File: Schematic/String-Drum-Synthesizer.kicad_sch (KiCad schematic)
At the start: 47 parts, among them J1 USB_A, J2 USB_A, J3 HDMI_A_1.4, U1 LM1117MP-3.3, U2 SII1136CTU, U4 LM3900DR, U5 LM1117MP-3.3, U6 STM32F722RCTx

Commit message: Schematic Done!!
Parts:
- removed C10: 4.7uF, symbol Device:C_Polarized
- added R18, R20, R22: 4k7, symbol Device:R
- added R19, R21, R23: 10k, symbol Device:R
- added R24, R25, R26: 1M, symbol Device:R
- added U3: 74LS257, symbol 74xx:74LS257
- renumbered AudioJack to AudioJack1, J1 to KeyboardUSBPort, J2 to ProgrammingUSBPort
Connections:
- net +5V: now also U3.16 (VCC), U3.2 (I0a); no longer J3.18 (+5V)
- net GND: now also R19.1, R21.1, R23.1, R24.1, R25.1, R26.1, U3.10 (I1d), U3.11 (I0d), U3.13 (I1c), U3.14 (I0c), U3.3 (I1a), U3.5 (I0b), U3.6 (I1b), U3.8 (GND)
- net PB10: now also U6.28 (PB10)
- net PB11: now also U6.29 (PB11)
- net PB2: now also U6.27 (PB2)
- net PB3: now also U6.55 (PB3)
- net PB4: now also U6.56 (PB4)
- net PB5: now also U6.57 (PB5)
- net PB6: now also U6.58 (PB6)
- net PB7: now also U6.59 (PB7)
- net PB8: now also U6.61 (PB8)
- net PB9: now also U6.62 (PB9)
- net PC0: now also U6.8 (PC0)
- net PC1: now also U6.9 (PC1)
- net PC13: now also U6.2 (PC13)
- net PC2: now also U6.10 (PC2)
- net USB_OTG_FS_DM: now also R10.2, R8.1; no longer KeyboardUSBPort.2 (D-)
- net USB_OTG_FS_DP: now also R22.1, R23.2; no longer KeyboardUSBPort.3 (D+)
- net USB_OTG_HS_DM: now also R20.1, R21.2; no longer ProgrammingUSBPort.2 (D-)
- net USB_OTG_HS_DP: now also R18.1, R19.2; no longer ProgrammingUSBPort.3 (D+)
- net HDMI_PWR: now reaches U6.50 (PA15)
- net HDMI_PWR: now also J3.18 (+5V), U3.4 (Za)
- net at R8.2: now also KeyboardUSBPort.2 (D-); no longer ProgrammingUSBPort.1 (VBUS)
- net USB_OTG_FS_VBUS: no longer names the net of U6.42 (PA9)
- removed net USB_OTG_HS_VBUS: R10.2, R8.1, U6.34 (PB13)
- new net: KeyboardUSBPort.3 (D+), R22.2
- new net: ProgrammingUSBPort.3 (D+), R18.2
- new net: R26.2, U3.9 (Zd)
- new net: ProgrammingUSBPort.2 (D-), R20.2
- new net: R25.2, U3.12 (Zc)
- new net: R24.2, U3.7 (Zb)
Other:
- moved on the sheet: ProgrammingUSBPort

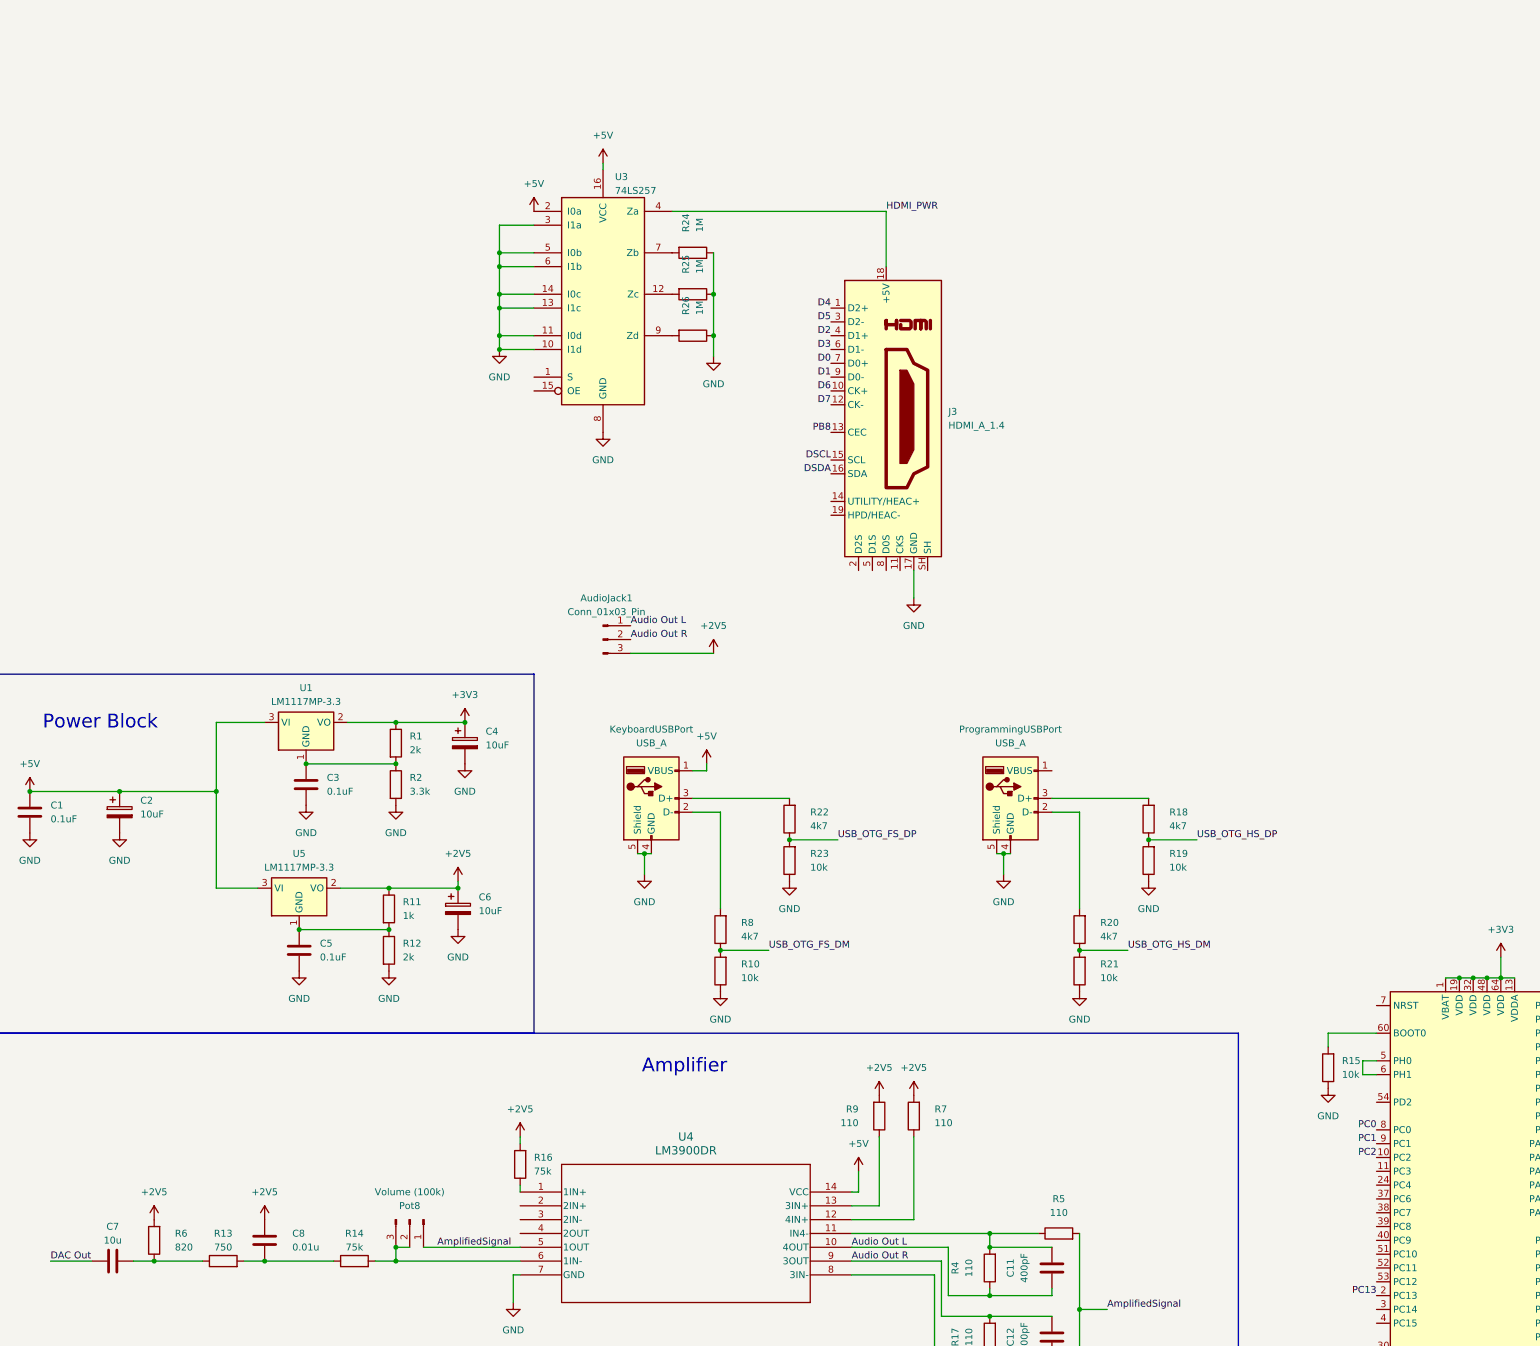
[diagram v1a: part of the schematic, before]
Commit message: Needs R and C Footprints
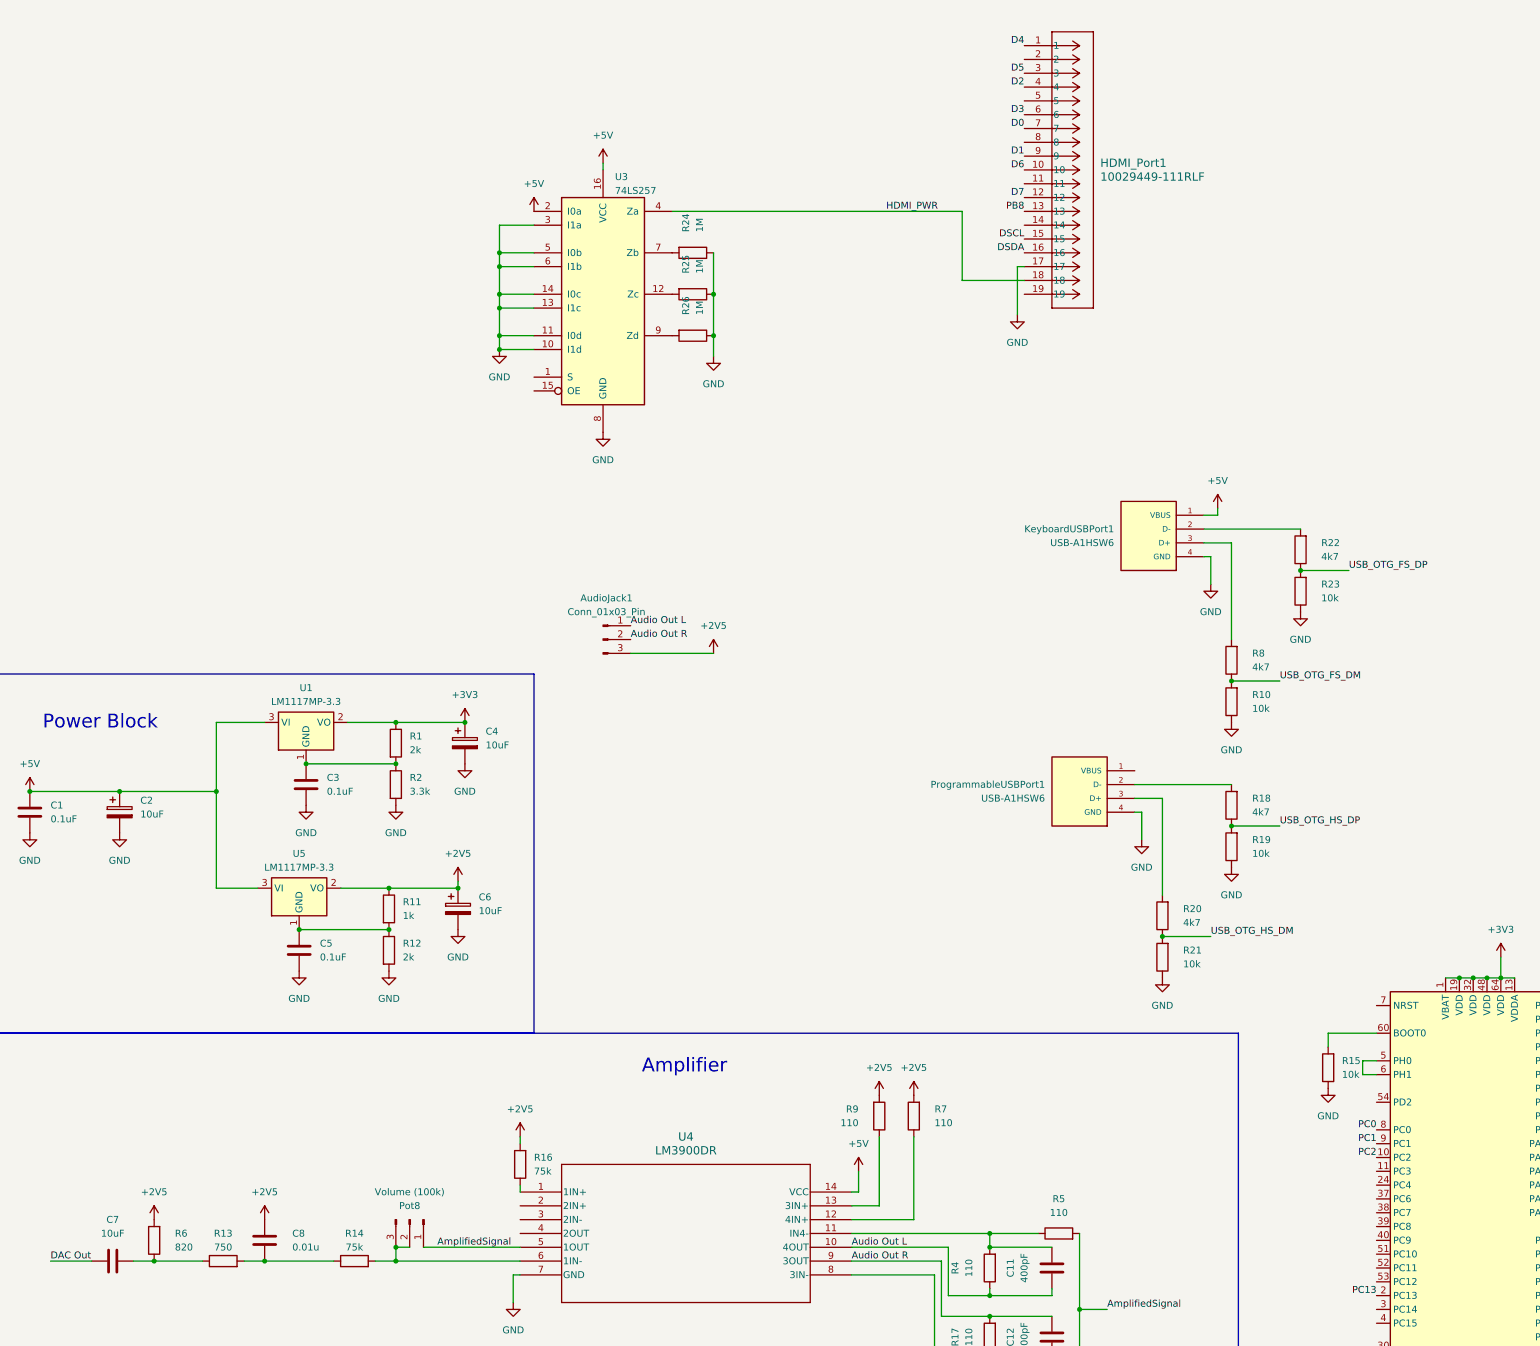
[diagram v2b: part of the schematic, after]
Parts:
- removed J3: HDMI_A_1.4, symbol Connector:HDMI_A_1.4
- removed KeyboardUSBPort, ProgrammingUSBPort: USB_A, symbol Connector:USB_A
- added HDMI_Port1: 10029449-111RLF, 10029449_111RLF:CONN_10029449111_AMP, symbol 10029449_111RLF:10029449-111RLF
- added KeyboardUSBPort1, ProgrammableUSBPort1: USB-A1HSW6, USB-A1HSW6:OST_USB-A1HSW6, symbol USB-A1HSW6:USB-A1HSW6
- AudioJack1, Pot0, Pot1, Pot2, Pot3, Pot4, Pot5, Pot6, Pot7, Pot8: footprint (none) -> Connector_Molex:Molex_KK-254_AE-6410-03A_1x03_P2.54mm_Vertical
- C7: value 10u -> 10uF
- U3: footprint (none) -> Package_DIP:DIP-16_W7.62mm_Socket
- U4: footprint D14 -> LM3900DR:D14
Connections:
- net +5V: now also KeyboardUSBPort1.1 (VBUS)
- net D0: now also HDMI_Port1.7
- net D1: now also HDMI_Port1.9
- net D2: now also HDMI_Port1.4
- net D3: now also HDMI_Port1.6
- net D4: now also HDMI_Port1.1
- net D5: now also HDMI_Port1.3
- net D6: now also HDMI_Port1.10
- net D7: now also HDMI_Port1.12
- net DSCL: now also HDMI_Port1.15
- net DSDA: now also HDMI_Port1.16
- net GND: now also HDMI_Port1.17, KeyboardUSBPort1.4 (GND), ProgrammableUSBPort1.4 (GND)
- net HDMI_PWR: now also HDMI_Port1.18
- net PB8: now also HDMI_Port1.13
- net at R8.2: now also KeyboardUSBPort1.3 (D+)
- net at R22.2: now also KeyboardUSBPort1.2 (D-)
- net at R18.2: now also ProgrammableUSBPort1.2 (D-)
- net at R20.2: now also ProgrammableUSBPort1.3 (D+)
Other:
- moved on the sheet: R10, R18, R19, R20, R21, R22, R23, R8

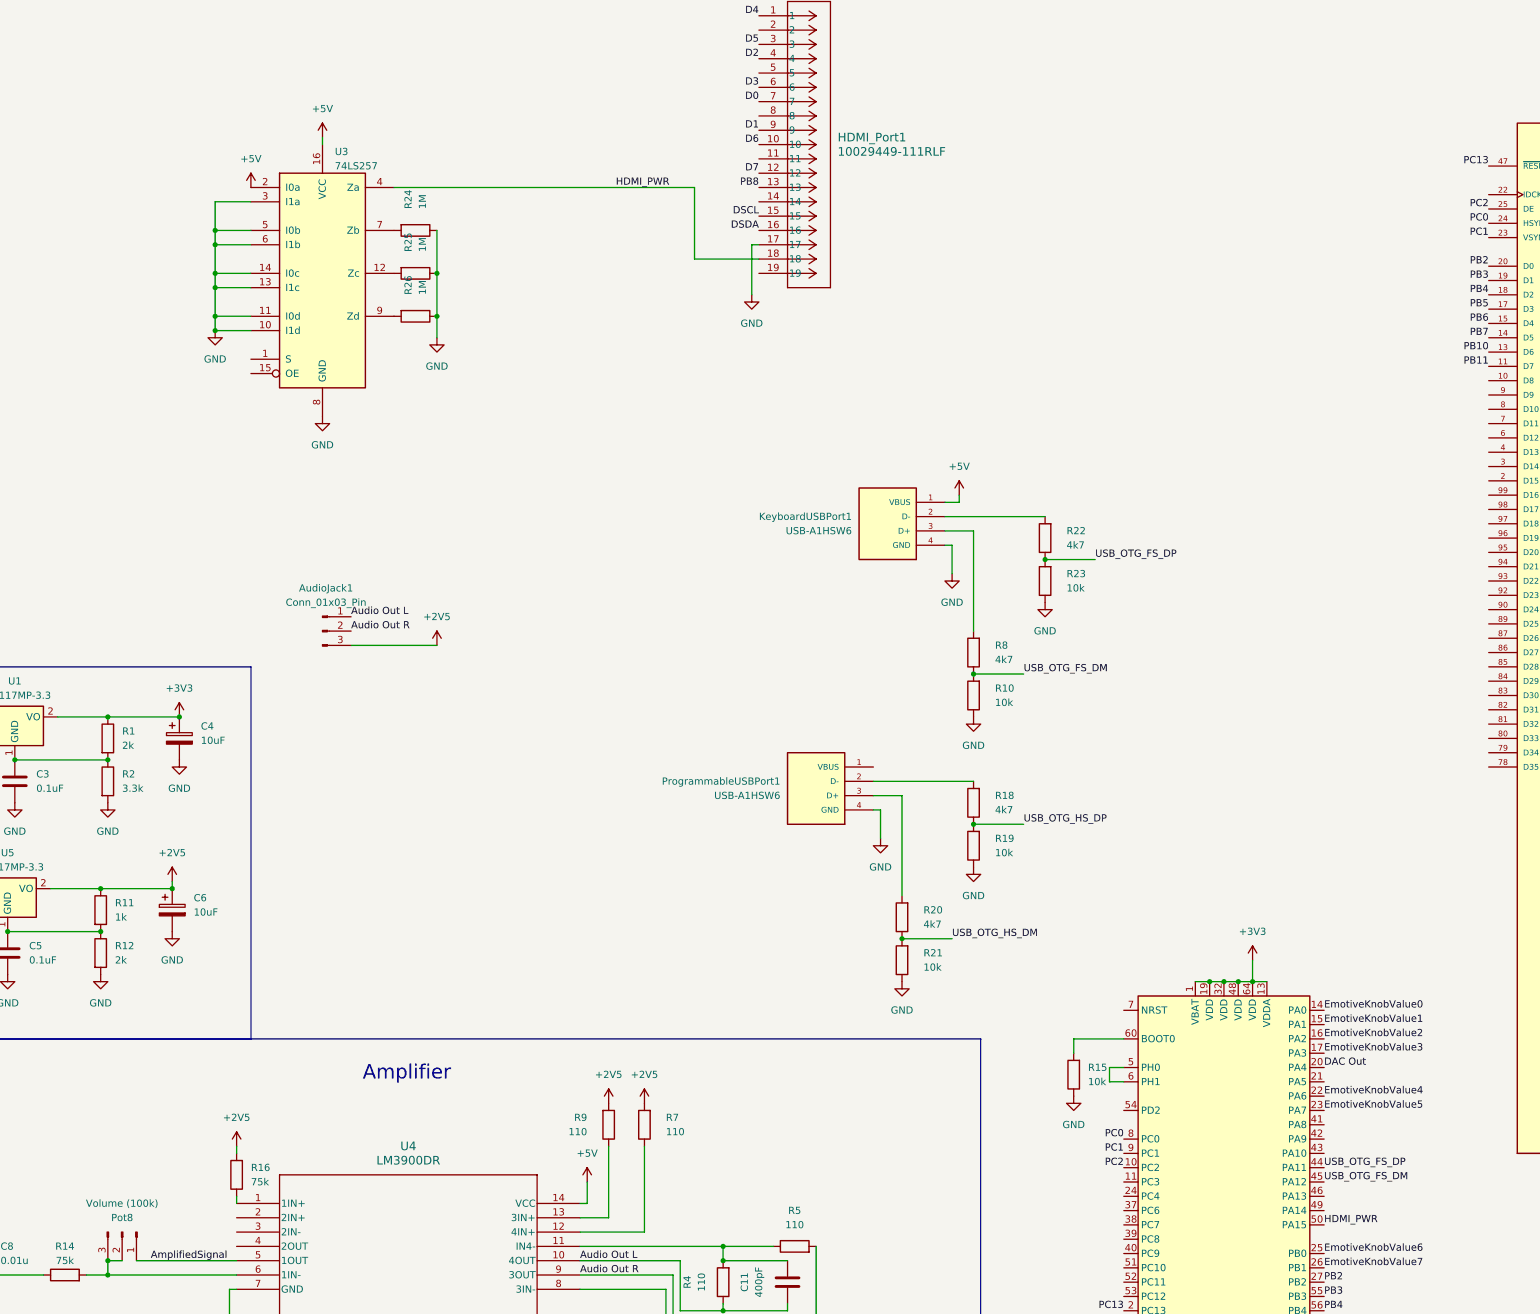
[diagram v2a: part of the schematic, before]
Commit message: Fixed multiplexor pinout
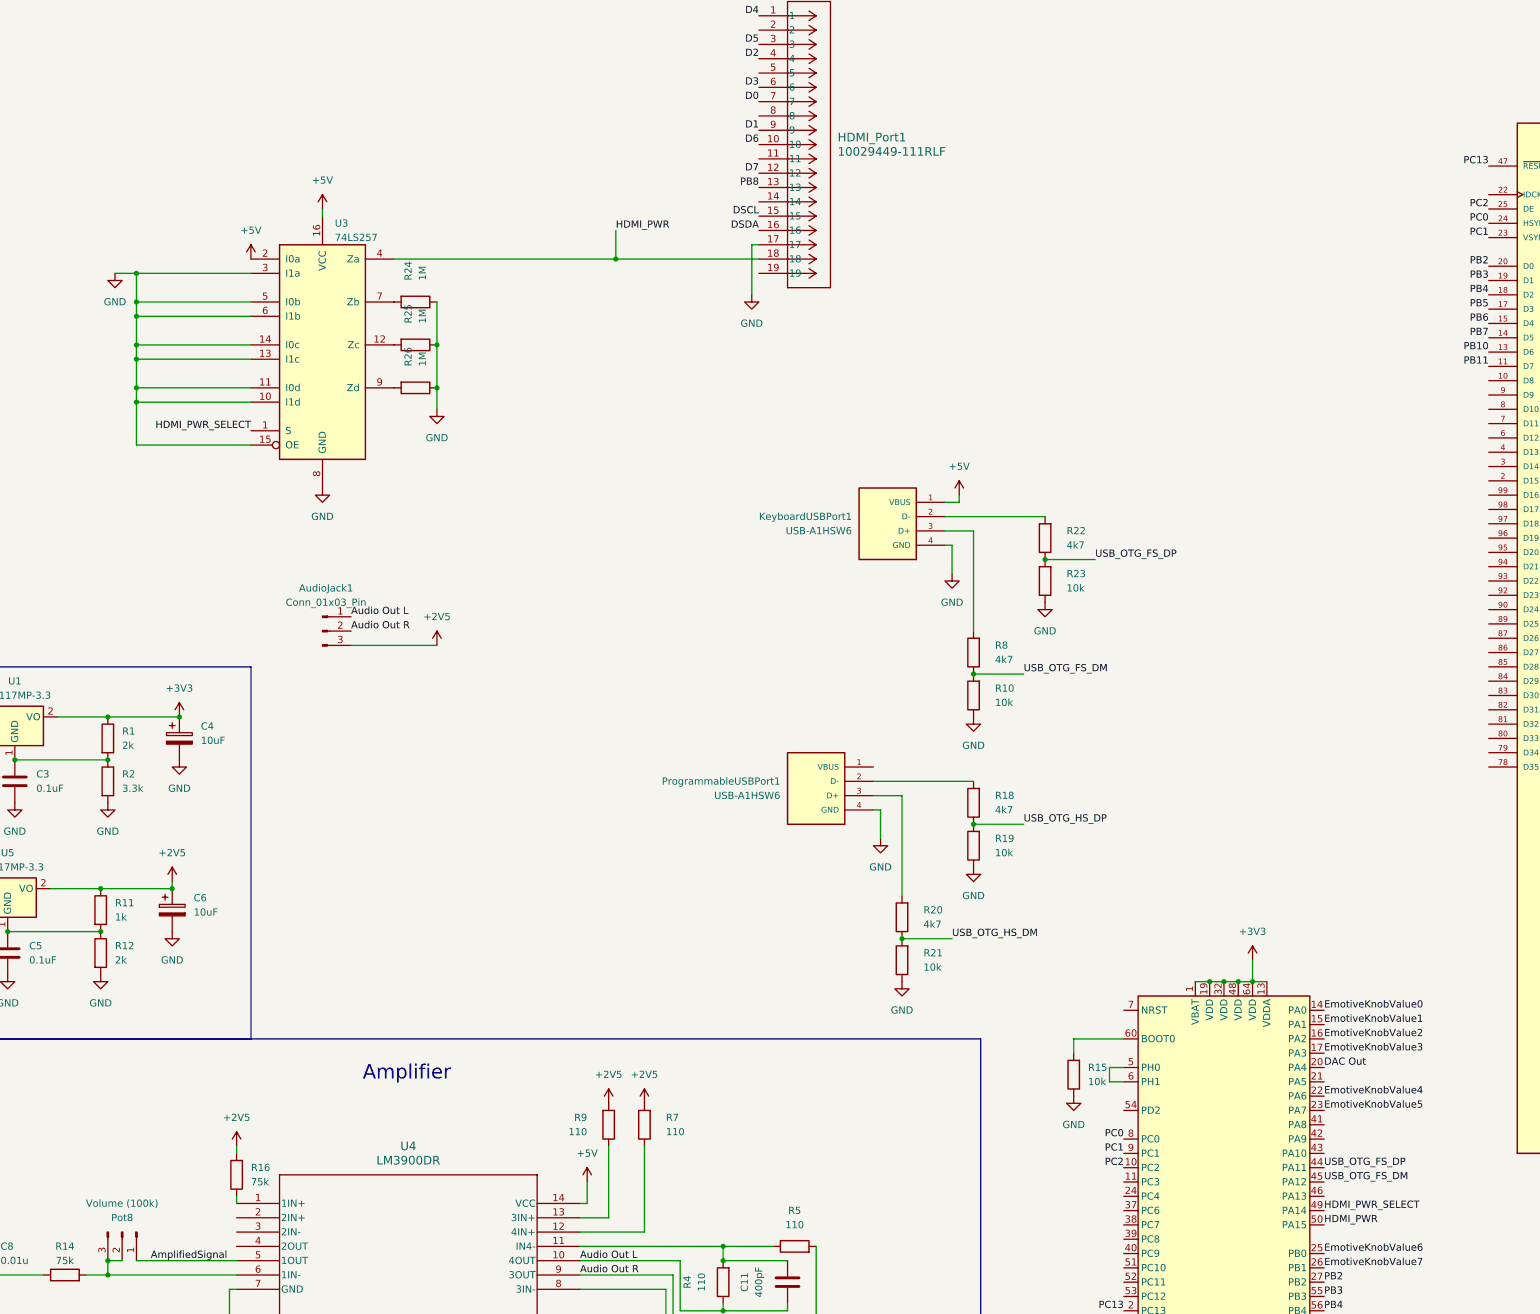
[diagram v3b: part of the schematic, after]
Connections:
- net GND: now also U3.15 (OE)
- net HDMI_PWR_SELECT: now reaches U6.49 (PA14)
- net HDMI_PWR_SELECT: now also U3.1 (S)
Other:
- moved on the sheet: R24, R25, R26, U3

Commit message: Fixed HDMI Pinout. Have to start PCB design over
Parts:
- added R27, R28, R29, R30, R31, R32: 220, Resistor_THT:R_Axial_DIN0207_L6.3mm_D2.5mm_P7.62mm_Horizontal, symbol Device:R
- C1, C11, C12, C3, C5, C8, C9: footprint (none) -> Capacitor_THT:C_Disc_D6.0mm_W4.4mm_P5.00mm
- C2, C4, C6, C7: footprint (none) -> Capacitor_THT:CP_Radial_D7.5mm_P2.50mm
- KeyboardUSBPort1, ProgrammableUSBPort1: footprint USB-A1HSW6:OST_USB-A1HSW6 -> USB_A1HSW6:OST_USB-A1HSW6
- R1, R10, R11, R12, R13, R14, R15, R16, R18, R19, R2, R20, R21, R22, R23, R24, R25, R26, R6, R8: footprint (none) -> Resistor_THT:R_Axial_DIN0207_L6.3mm_D2.5mm_P7.62mm_Horizontal
- R17, R3, R4, R5, R7, R9: value 110 -> 220; footprint (none) -> Resistor_THT:R_Axial_DIN0207_L6.3mm_D2.5mm_P7.62mm_Horizontal
- U2: footprint SII1136CTU:QFP50P1600X1600X120-101N -> Package_QFP:TQFP-100-1EP_14x14mm_P0.5mm_EP5x5mm
- U4: footprint LM3900DR:D14 -> Package_DIP:DIP-14_W7.62mm_Socket
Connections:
- net D0 is gone; now on net PB2: HDMI_Port1.7
- net D1 is gone; now on net PB3: HDMI_Port1.9
- net D2 is gone; now on net PB4: HDMI_Port1.4
- net D3 is gone; now on net PB5: HDMI_Port1.6
- net D4 is gone; now on net PB6: HDMI_Port1.1
- net D5 is gone; now on net PB7: HDMI_Port1.3
- net D6 is gone; now on net PB10: HDMI_Port1.10
- net D7 is gone; now on net PB11: HDMI_Port1.12
- net +2V5: now also R31.2, R32.2
- net AmplifiedSignal: now also R29.2, R30.2
- net Audio Out L: now also R28.1
- net Audio Out R: now also R27.2
- net DSCL: now also U2.42 (DSCL)
- net DSDA: now also U2.41 (DSDA)
- net PB8: no longer HDMI_Port1.13, U2.42 (DSCL)
- net PB9: no longer U2.41 (DSDA)
- net CEC_A: now reaches U2.40 (CEC_A)
- net CEC_A: now also HDMI_Port1.13
- net at C11.2, R4.2, R5.1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: now also R28.2, R29.1
- net at R7.1, U4.12 (4IN+): now also R32.1
- net at R9.1, U4.13 (3IN+): now also R31.1
- net at C12.1, R17.1, R3.1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: now also R27.1, R30.1
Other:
- moved on the sheet: AudioJack1, C1, C11, C12, C2, C3, C4, C5, C6, C7, C8, C9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
